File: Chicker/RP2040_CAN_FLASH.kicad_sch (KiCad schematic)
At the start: 65 parts, among them J1 JST_B3B-XH-A, J2 USB4145-03-0170-C_REVA2, J3 JST_BM04B-GHS-TBT, J4 EG1206, J5 Conn_02x10_Counter_Clockwise, Q1 BSS138, Q4 BSS138, U1 RPI2040, U10 PTS647SM38SMTR2LFS, U5 W25Q16JVSNIQ, U6 SN65HVD233, U7 MCP2515-xST, U9 PTS647SM38SMTR2LFS, Y1 ABM3-12.000MHZ-D2Y-T, Y2 ABM3-8.000MHZ-D2Y-T

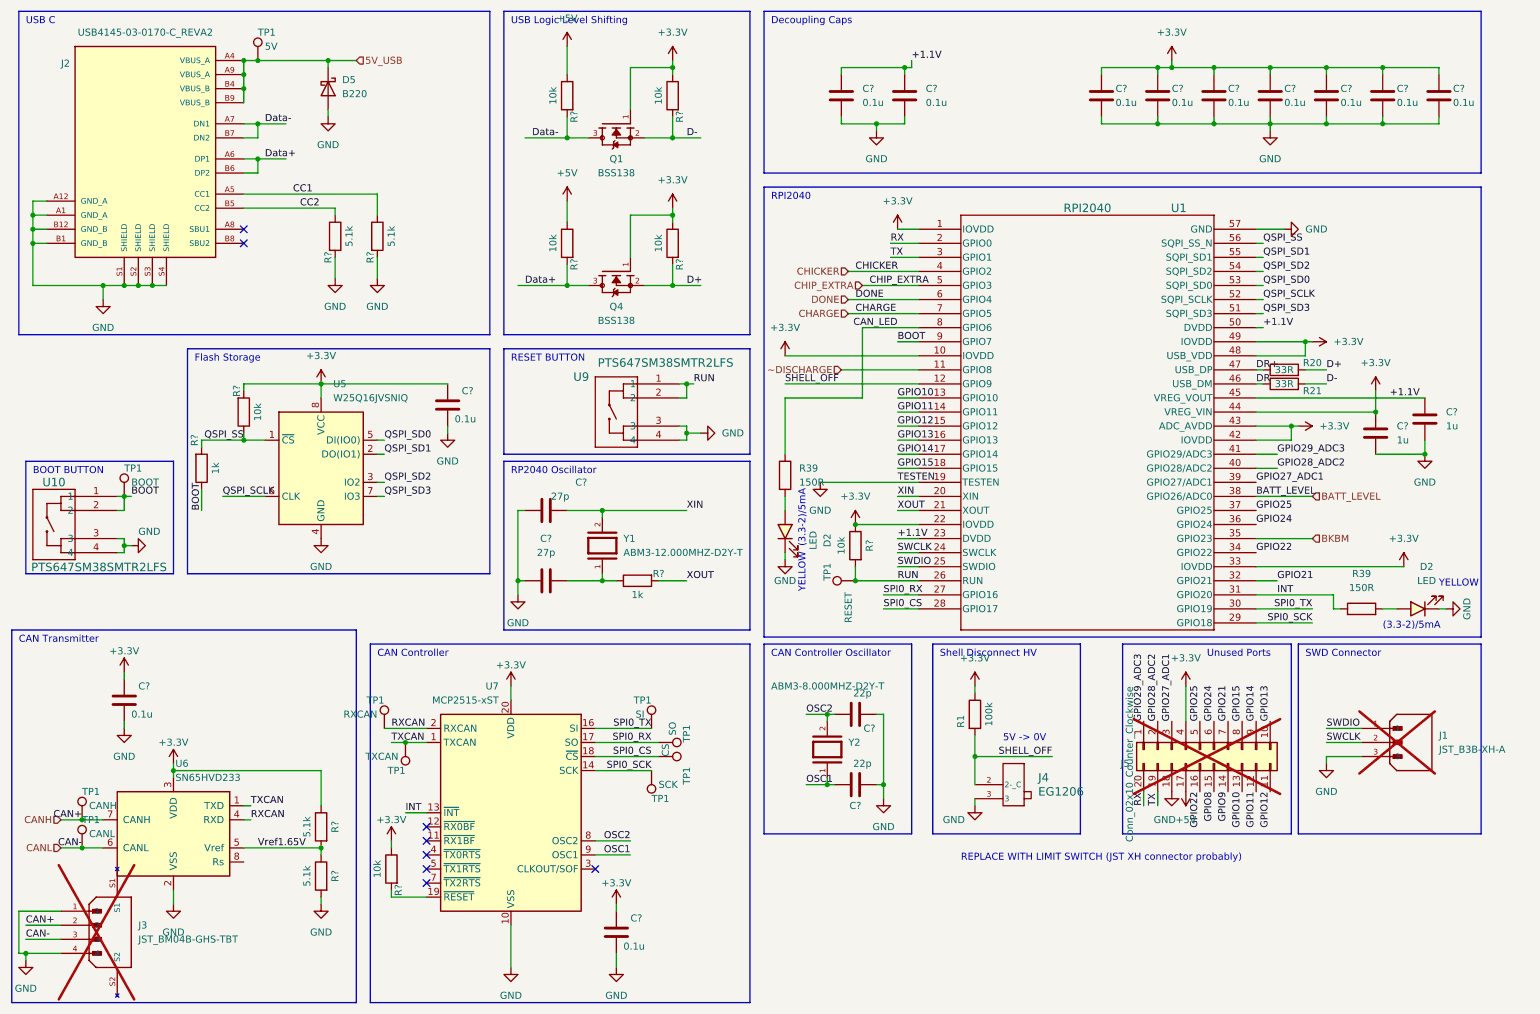
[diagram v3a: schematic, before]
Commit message: chicker discharge circuit finalized
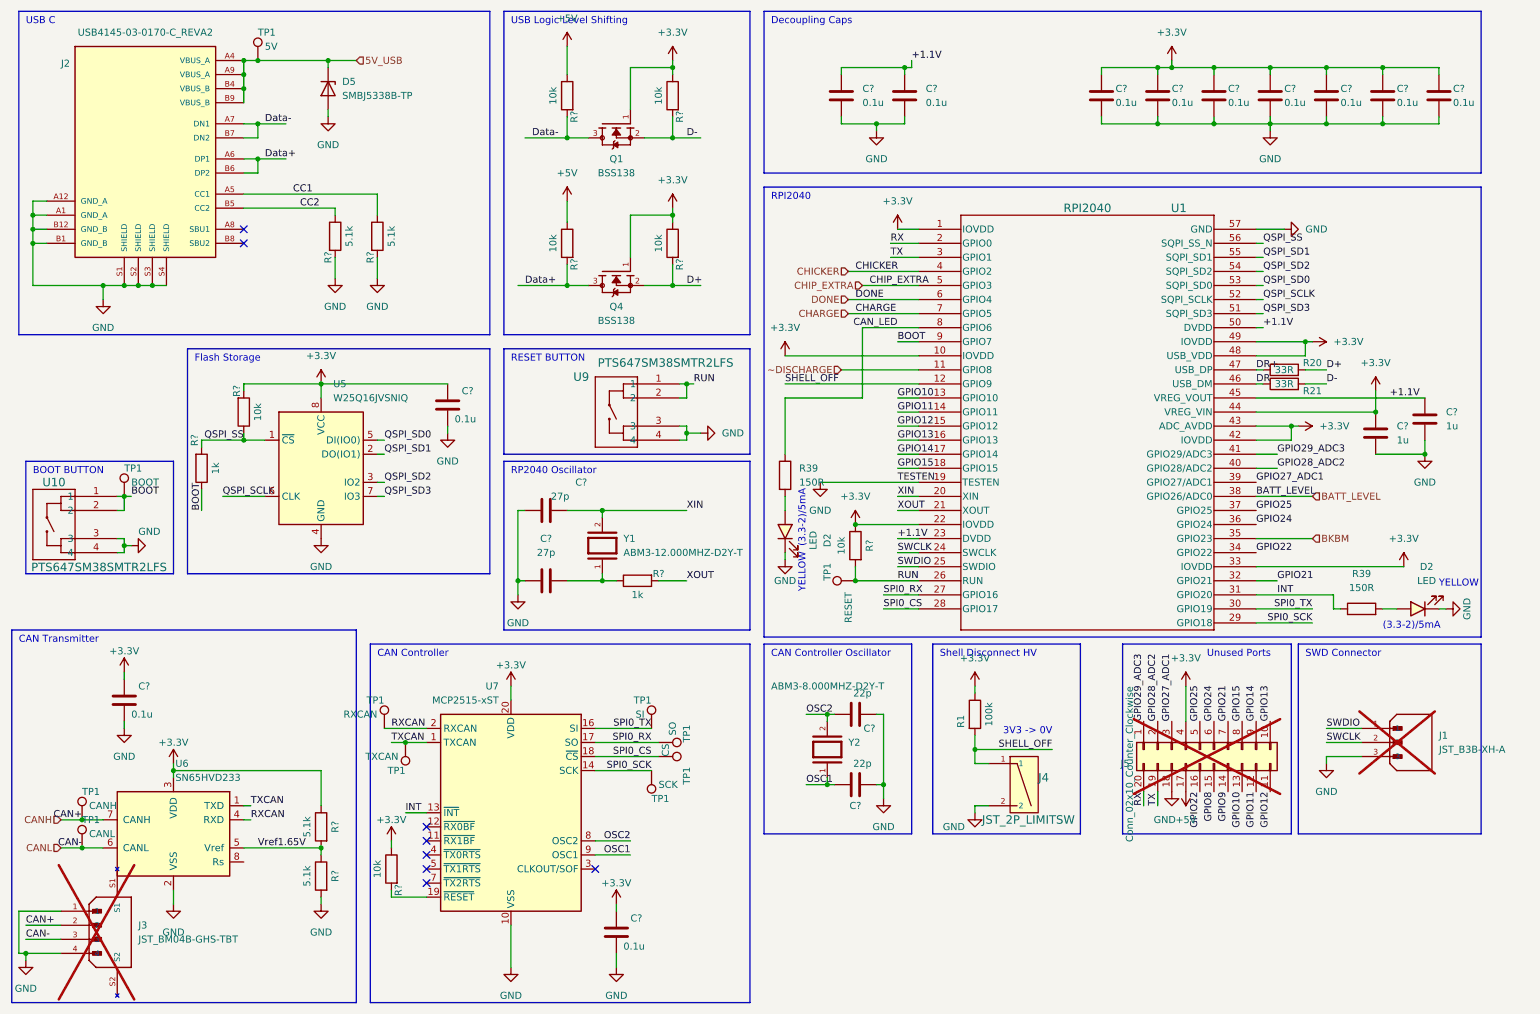
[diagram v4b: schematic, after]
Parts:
- removed D5: B220, bots:D_SMB, symbol bots:B220
- removed J4: EG1206, bots:SW_EG1206, symbol bots:SW_EG1206
- added D5: SMBJ5338B-TP, bots:D_SMB, symbol bots:D_ZENER_SMBJ5338B-TP
- added J4: JST_2P_LIMITSW, bots:JST_B2B-XH-A_LF__SN_, symbol bots:JST_TO_LIMITSW
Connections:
- net 5V_USB: now also D5.1 (K)
- net GND: now also D5.2 (A), J4.2
- net SHELL_OFF: now also J4.1
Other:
- note added: "3V3 -> 0V"
- note removed: "5V -> 0V"
- note removed: "REPLACE WITH LIMIT SWITCH (JST XH connector probably)"
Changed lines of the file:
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@@
   (junction (at 251.46 25.4) (diameter 0) (color 0 0 0 0)
   )
+  (junction (at 187.96 148.59) (diameter 0) (color 0 0 0 0)
+  )
   (junction (at 26.67 166.37) (diameter 0) (color 0 0 0 0)
   )
@@
   (junction (at 175.26 25.4) (diameter 0) (color 0 0 0 0)
   )
-  (junction (at 187.96 149.86) (diameter 0) (color 0 0 0 0)
-  )
   (junction (at 135.89 91.44) (diameter 0) (color 0 0 0 0)
   )
@@
     (stroke (width 0) (type default))
   )
+  (wire (pts (xy 187.96 160.02) (xy 187.96 158.75))
+    (stroke (width 0) (type default))
+  )
   (wire (pts (xy 260.35 95.25) (xy 269.24 95.25))
     (stroke (width 0) (type default))
@@
     (stroke (width 0) (type default))
   )
-  (wire (pts (xy 187.96 149.86) (xy 201.93 149.86))
+  (wire (pts (xy 187.96 148.59) (xy 201.93 148.59))
     (stroke (width 0) (type default))
   )
@@
     (stroke (width 0) (type default))
   )
-  (wire (pts (xy 187.96 157.48) (xy 187.96 158.75))
-    (stroke (width 0) (type default))
-  )
   (wire (pts (xy 80.01 92.71) (xy 81.28 92.71))
     (stroke (width 0) (type default))
@@
     (stroke (width 0) (type default))
   )
+  (wire (pts (xy 190.5 151.13) (xy 187.96 151.13))
+    (stroke (width 0) (type default))
+  )
   (wire (pts (xy 173.99 54.61) (xy 177.8 54.61))
     (stroke (width 0) (type default))
   )
-  (wire (pts (xy 187.96 146.05) (xy 187.96 149.86))
+  (wire (pts (xy 187.96 146.05) (xy 187.96 148.59))
     (stroke (width 0) (type default))
   )
@@
     (stroke (width 0) (type default))
   )
+  (wire (pts (xy 187.96 148.59) (xy 187.96 151.13))
+    (stroke (width 0) (type default))
+  )
   (wire (pts (xy 58.42 44.45) (xy 58.42 41.91))
     (stroke (width 0) (type default))
@@
     (stroke (width 0) (type default))
   )
-  (wire (pts (xy 187.96 149.86) (xy 187.96 154.94))
-    (stroke (width 0) (type default))
-  )
   (wire (pts (xy 33.02 105.41) (xy 34.29 105.41))
     (stroke (width 0) (type default))
@@
     (stroke (width 0) (type default))
   )
+  (wire (pts (xy 187.96 158.75) (xy 190.5 158.75))
+    (stroke (width 0) (type default))
+  )
   (wire (pts (xy 238.76 80.01) (xy 240.03 80.01))
     (stroke (width 0) (type default))
@@
     (effects (font (size 1.27 1.27)) (justify left bottom))
   )
-  (text "5V -> 0V" (at 193.04 147.32 0)
+  (text "3V3 -> 0V" (at 193.04 146.05 0)
     (effects (font (size 1.27 1.27)) (justify left bottom))
   )
@@
     (effects (font (size 1.27 1.27) (color 0 4 0 1)) (justify left bottom))
   )
-  (text "REPLACE WITH LIMIT SWITCH (JST XH connector probably)"
-    (at 185.42 168.91 0)
-    (effects (font (size 1.27 1.27) (color 255 0 0 1)) (justify left bottom))
-  )
   (label "SPI0_CS" (at 171.45 123.19 0) (fields_autoplaced)
     (effects (font (size 1.27 1.27)) (justify left bottom))
@@
     (effects (font (size 1.27 1.27)) (justify left bottom))
   )
-  (label "SHELL_OFF" (at 201.93 149.86 180) (fields_autoplaced)
+  (label "SHELL_OFF" (at 201.93 148.59 180) (fields_autoplaced)
     (effects (font (size 1.27 1.27)) (justify right bottom))
   )
@@
     )
   )
+  (symbol (lib_id "bots:JST_TO_LIMITSW") (at 195.58 154.94 0) (unit 1)
+    (in_bom yes) (on_board yes) (dnp no)
+    (property "Reference" "J4" (at 199.39 153.67 0)
+      (effects (font (size 1.524 1.524)) (justify left))
+    )
+    (property "Value" "JST_2P_LIMITSW" (at 189.23 161.29 0)
+      (effects (font (size 1.524 1.524)) (justify left))
+    )
+    (property "Footprint" "bots:JST_B2B-XH-A_LF__SN_" (at 195.58 140.97 0)
+      (effects (font (size 1.27 1.27) italic) hide)
+    )
+    (property "Datasheet" "" (at 195.58 143.51 0)
+      (effects (font (size 1.27 1.27) italic) hide)
+    )
+    (pin "1")
+    (pin "2")
+    (instances
+      (project "chicker"
+        (path "/1a9ce3e8-a091-496c-9c5f-e7b2eb60e275/44109b35-87db-4b37-b749-86ba1243ffef"
+          (reference "J4") (unit 1)
+        )
+      )
+    )
+  )
   (symbol (lib_id "bots:TestPoint_1x1") (at 130.81 147.32 270) (mirror x) (unit 1)
     (in_bom no) (on_board yes) (dnp no)
@@
     )
   )
+  (symbol (lib_id "bots:D_ZENER_SMBJ5338B-TP") (at 71.12 29.21 270) (unit 1)
+    (in_bom yes) (on_board yes) (dnp no) (fields_autoplaced)
+    (property "Reference" "D5" (at 73.66 27.94 90)
+      (effects (font (size 1.27 1.27)) (justify left))
+    )
+    (property "Value" "SMBJ5338B-TP" (at 73.66 30.48 90)
+      (effects (font (size 1.27 1.27)) (justify left))
+    )
+    (property "Footprint" "bots:D_SMB" (at 71.12 29.21 0)
+      (effects (font (size 1.27 1.27)) hide)
+    )
+    (property "Datasheet" "~" (at 71.12 29.21 0)
+      (effects (font (size 1.27 1.27)) hide)
+    )
+    (property "MPN" "SMBJ5338B-TP" (at 71.12 29.21 0)
+      (effects (font (size 1.27 1.27)) hide)
+    )
+    (property "Manufacturer" "Micro Commercial Co" (at 71.12 29.21 0)
+      (effects (font (size 1.27 1.27)) hide)
+    )
+    (property "Price" "0.25" (at 71.12 29.21 0)
+      (effects (font (size 1.27 1.27)) hide)
+    )
+    (property "JLC" "DO-214AA(SMB)" (at 71.12 29.21 0)
+      (effects (font (size 1.27 1.27)) hide)
+    )
+    (property "LCSC" "C457823" (at 71.12 29.21 0)
+      (effects (font (size 1.27 1.27)) hide)
+    )
+    (property "JLC Extended" "yes" (at 71.12 29.21 0)
+      (effects (font (size 1.27 1.27)) hide)
+    )
+    (pin "1")
+    (pin "2")
+    (instances
+      (project "chicker"
+        (path "/1a9ce3e8-a091-496c-9c5f-e7b2eb60e275/44109b35-87db-4b37-b749-86ba1243ffef"
+          (reference "D5") (unit 1)
+        )
+      )
+    )
+  )
   (symbol (lib_id "power:+3.3V") (at 133.35 50.8 0) (mirror y) (unit 1)
     (in_bom yes) (on_board yes) (dnp no) (fields_autoplaced)
@@
     )
   )
-  (symbol (lib_id "bots:B220") (at 71.12 29.21 270) (unit 1)
-    (in_bom yes) (on_board yes) (dnp no) (fields_autoplaced)
-    (property "Reference" "D5" (at 73.66 27.6225 90)
-      (effects (font (size 1.27 1.27)) (justify left))
-    )
-    (property "Value" "B220" (at 73.66 30.1625 90)
-      (effects (font (size 1.27 1.27)) (justify left))
-    )
-    (property "Footprint" "bots:D_SMB" (at 66.675 29.21 0)
-      (effects (font (size 1.27 1.27)) hide)
-    )
-    (property "Datasheet" "http://www.jameco.com/Jameco/Products/ProdDS/1538777.pdf" (at 71.12 29.21 0)
-      (effects (font (size 1.27 1.27)) hide)
-    )
-    (property "MPN" "B220-13-F" (at 71.12 29.21 0)
-      (effects (font (size 1.27 1.27)) hide)
-    )
-    (property "Manufacturer" "Diodes Incorporated" (at 71.12 29.21 0)
-      (effects (font (size 1.27 1.27)) hide)
-    )
-    (property "Price" "0.0833" (at 71.12 29.21 0)
-      (effects (font (size 1.27 1.27)) hide)
-    )
-    (property "JLC" "SMB(DO-214AA)" (at 71.12 29.21 0)
-      (effects (font (size 1.27 1.27)) hide)
-    )
-    (property "LCSC" "C110480" (at 71.12 29.21 0)
-      (effects (font (size 1.27 1.27)) hide)
-    )
-    (pin "1")
-    (pin "2")
-    (instances
-      (project "chicker"
-        (path "/1a9ce3e8-a091-496c-9c5f-e7b2eb60e275/44109b35-87db-4b37-b749-86ba1243ffef"
-          (reference "D5") (unit 1)
-        )
-        (path "/1a9ce3e8-a091-496c-9c5f-e7b2eb60e275/13b16574-f046-4bb6-b573-f06681d59f31"
-          (reference "D5") (unit 1)
-        )
-      )
-    )
-  )
   (symbol (lib_id "bots:JST_B3B-XH-A") (at 262.89 147.32 0) (unit 1)
     (in_bom no) (on_board yes) (dnp yes) (fields_autoplaced)
@@
     )
   )
-  (symbol (lib_id "power:GND") (at 187.96 158.75 0) (unit 1)
+  (symbol (lib_id "power:GND") (at 187.96 160.02 0) (unit 1)
     (in_bom yes) (on_board yes) (dnp no)
-    (property "Reference" "#PWR?" (at 187.96 165.1 0)
+    (property "Reference" "#PWR?" (at 187.96 166.37 0)
       (effects (font (size 1.27 1.27)) hide)
     )
-    (property "Value" "GND" (at 184.15 161.29 0)
+    (property "Value" "GND" (at 184.15 162.56 0)
       (effects (font (size 1.27 1.27)))
     )
-    (property "Footprint" "" (at 187.96 158.75 0)
+    (property "Footprint" "" (at 187.96 160.02 0)
       (effects (font (size 1.27 1.27)) hide)
     )
-    (property "Datasheet" "" (at 187.96 158.75 0)
+    (property "Datasheet" "" (at 187.96 160.02 0)
       (effects (font (size 1.27 1.27)) hide)
     )
@@
         )
       )
-    )
-  )
-  (symbol (lib_id "bots:SW_EG1206") (at 194.31 153.67 0) (unit 1)
-    (in_bom yes) (on_board yes) (dnp no) (fields_autoplaced)
-    (property "Reference" "J4" (at 199.39 153.67 0)
-      (effects (font (size 1.524 1.524)) (justify left))
-    )
-    (property "Value" "EG1206" (at 199.39 156.21 0)
-      (effects (font (size 1.524 1.524)) (justify left))
-    )
-    (property "Footprint" "bots:SW_EG1206" (at 194.31 139.7 0)
-      (effects (font (size 1.27 1.27) italic) hide)
-    )
-    (property "Datasheet" "" (at 194.31 142.24 0)
-      (effects (font (size 1.27 1.27) italic) hide)
-    )
-    (pin "2")
-    (pin "3")
-    (pin "1")
-    (pin "SH1")
-    (pin "SH2")
-    (instances
-      (project "chicker"
-        (path "/1a9ce3e8-a091-496c-9c5f-e7b2eb60e275/44109b35-87db-4b37-b749-86ba1243ffef"
-          (reference "J4") (unit 1)
-        )
-      )

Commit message: chicker v1.1 changes
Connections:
- net GPIO8 is gone; now on net ~DISCHARGE: J5.15 (Pin_15)
- net GPIO9 is gone; now on net SHELL_OFF: J5.14 (Pin_14)
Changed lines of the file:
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@@
     (effects (font (size 1.27 1.27)) (justify left bottom))
+  )
+  (label "SHELL_OFF" (at 233.68 156.21 270) (fields_autoplaced)
+    (effects (font (size 1.27 1.27)) (justify right bottom))
   )
   (label "GPIO28_ADC2" (at 242.57 97.79 0) (fields_autoplaced)
     (effects (font (size 1.27 1.27)) (justify left bottom))
   )
+  (label "~DISCHARGE" (at 231.14 156.21 270) (fields_autoplaced)
+    (effects (font (size 1.27 1.27)) (justify right bottom))
+  )
   (label "RXCAN" (at 57.15 161.29 0) (fields_autoplaced)
     (effects (font (size 1.27 1.27)) (justify left bottom))
@@
     (effects (font (size 1.27 1.27)) (justify left bottom))
   )
-  (label "GPIO9" (at 233.68 156.21 270) (fields_autoplaced)
-    (effects (font (size 1.27 1.27)) (justify right bottom))
-  )
   (label "Vref1.65V" (at 58.42 166.37 0) (fields_autoplaced)
     (effects (font (size 1.27 1.27)) (justify left bottom))
@@
     (effects (font (size 1.27 1.27)) (justify left bottom))
   )
+  (label "~DISCHARGE" (at 168.91 80.01 0) (fields_autoplaced)
+    (effects (font (size 1.27 1.27)) (justify left bottom))
+  )
   (label "TX" (at 172.72 59.69 0) (fields_autoplaced)
     (effects (font (size 1.27 1.27)) (justify left bottom))
@@
     (effects (font (size 1.27 1.27)) (justify left bottom))
   )
-  (label "GPIO8" (at 231.14 156.21 270) (fields_autoplaced)
-    (effects (font (size 1.27 1.27)) (justify right bottom))
-  )
   (label "Data-" (at 59.69 35.56 0) (fields_autoplaced)

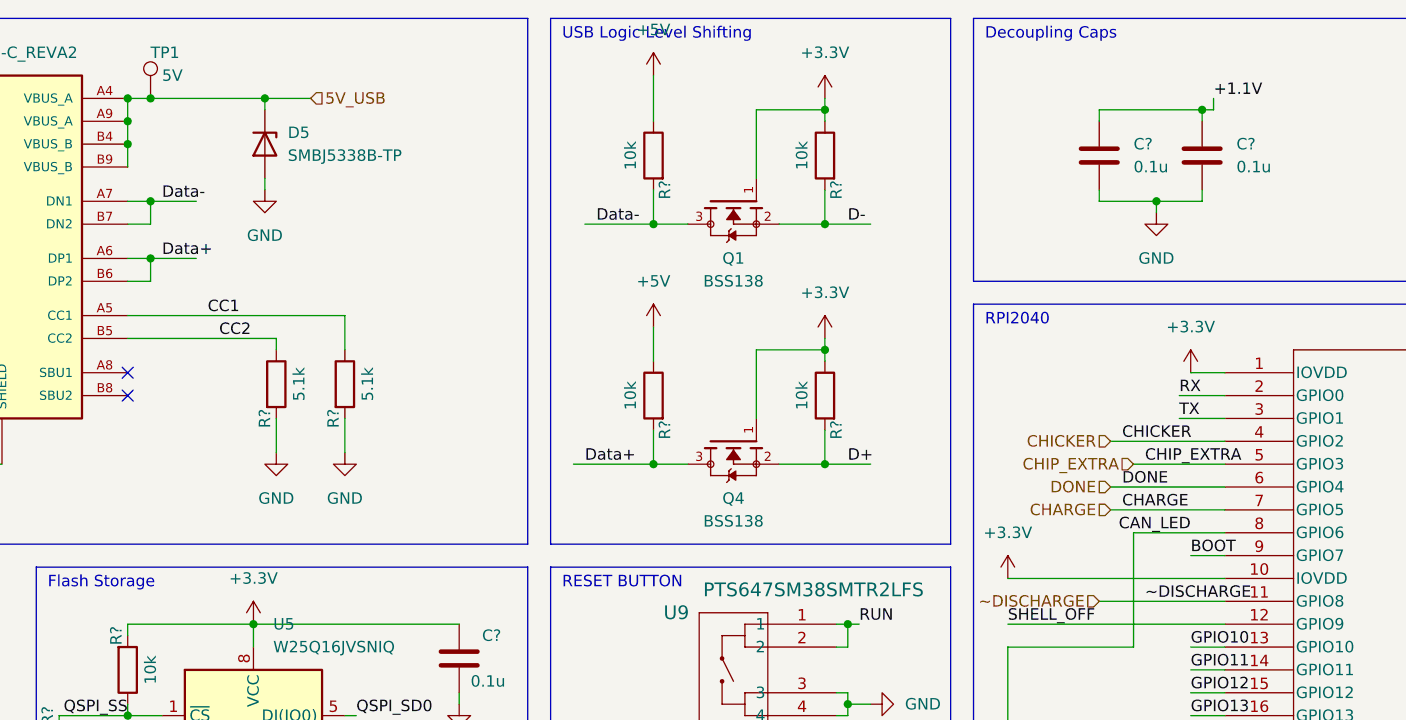
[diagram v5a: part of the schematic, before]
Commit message: added a global library for symbols
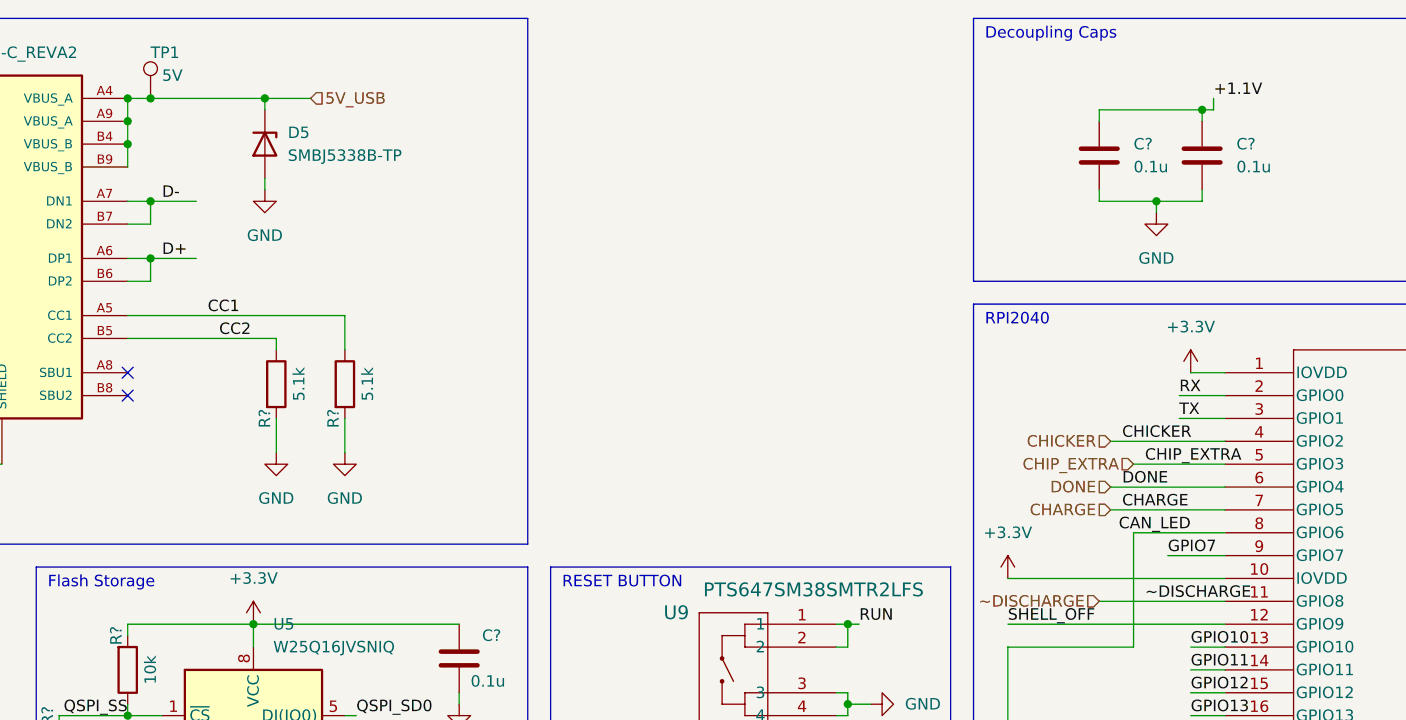
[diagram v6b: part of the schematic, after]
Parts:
- removed Q1, Q4: BSS138, bots:SOT95P240X111-3N, symbol bots:BSS138
- removed R? (x4): 10k, bots:R_0603_1608Metric, symbol bots:R_10k
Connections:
- net Data+ is gone; now on net D+: J2.A6 (DP1), J2.B6 (DP2)
- net Data- is gone; now on net D-: J2.A7 (DN1), J2.B7 (DN2)
- net BOOT: no longer U1.9 (GPIO7)
- new net GPIO7: U1.9 (GPIO7)
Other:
- note removed: "USB Logic Level Shifting"
